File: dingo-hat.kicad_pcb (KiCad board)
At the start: 2 copper layers, 65 x 56 mm, 94 parts, among them J1 LiPo-Power, J10 PJ-038BH, J11 Bypass-Power, J12 Chassis-Out, J13 i2c_display, J14 NEOPIXEL, J15 MPU-9250, J2 Raspberry_Pi_2_3, J201 Bootstrap, J24 3mm_Mount, J25 3mm_Mount, J26 3mm_Mount, J27 3mm_Mount, J3 ULTRA_0, J4 ULTRA_1, J5 LiPo-Balance, J6 0, J7 1, J8 2, J9 3, SW1 GPIO13, U1 MCP3021, U2 PCA9685PW, U201 AP9211, U202 MCP73213T, U203 BQ29209DRBR, U301 AOZ6605PI-1

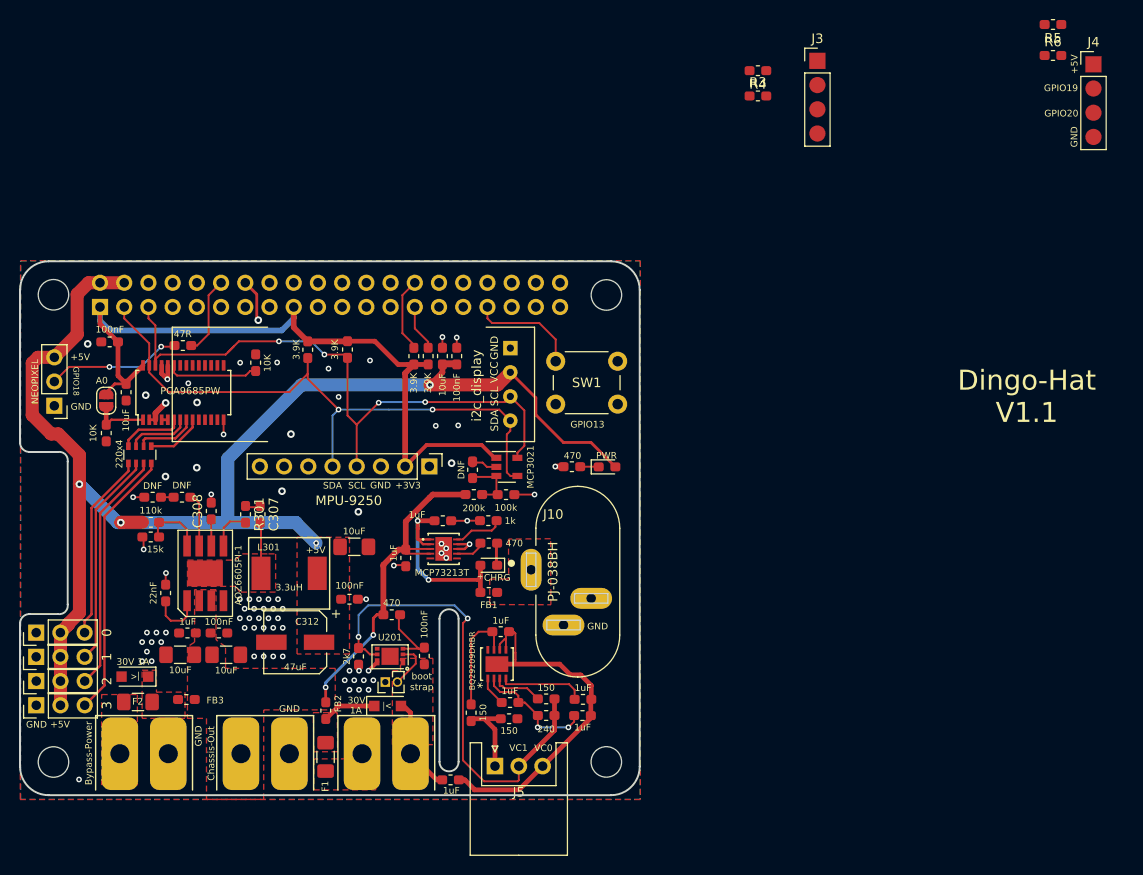
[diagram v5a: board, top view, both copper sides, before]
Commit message: Minor updates to hopefully make soldering easier.
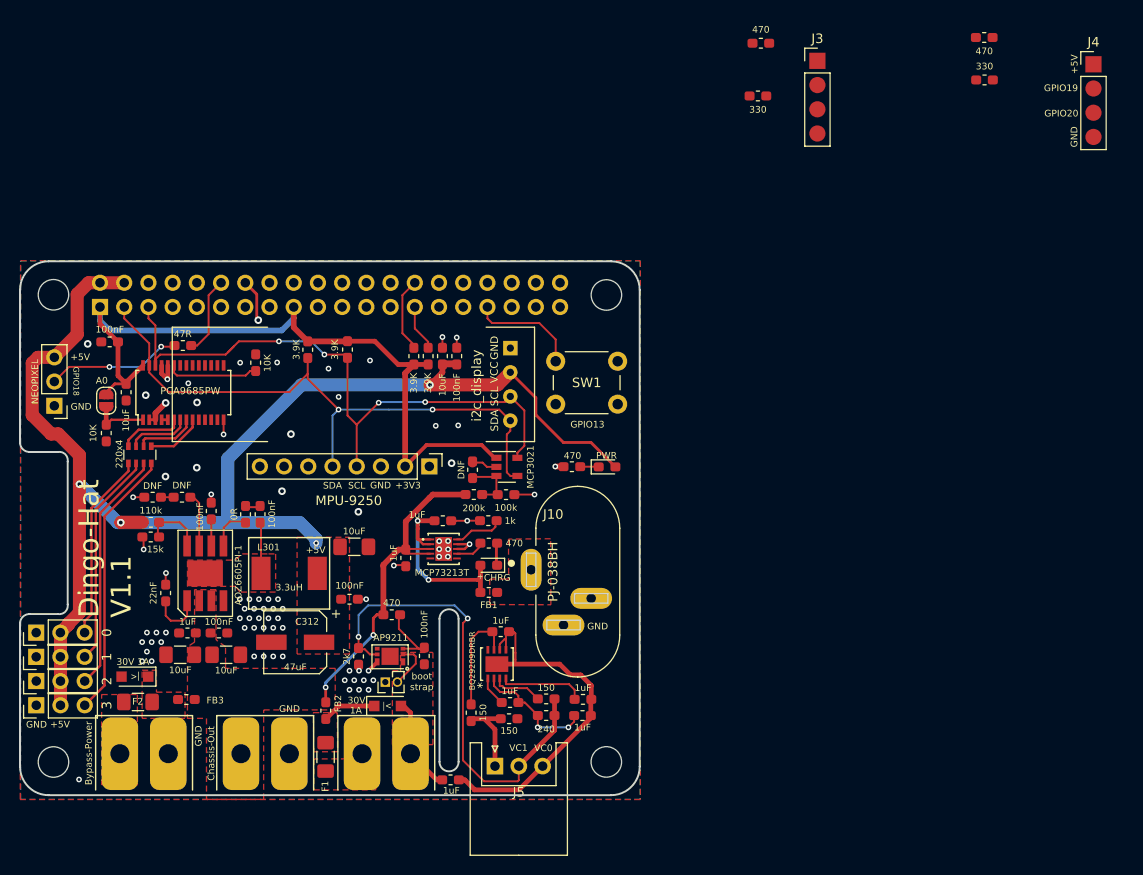
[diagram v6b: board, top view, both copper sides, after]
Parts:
- moved G4 85.2 mm to (186.8, 52.0)
- moved G5 85.2 mm to (186.7, 52.0)
- moved R5 9.24 mm to (201.2, 24.5)
- moved R6 7.45 mm to (201.1, 20.0)
- moved R4 2.90 mm to (177.7, 20.6)
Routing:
- net GND: vias 81 -> 83

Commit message: Tweaks to footprint alignment.
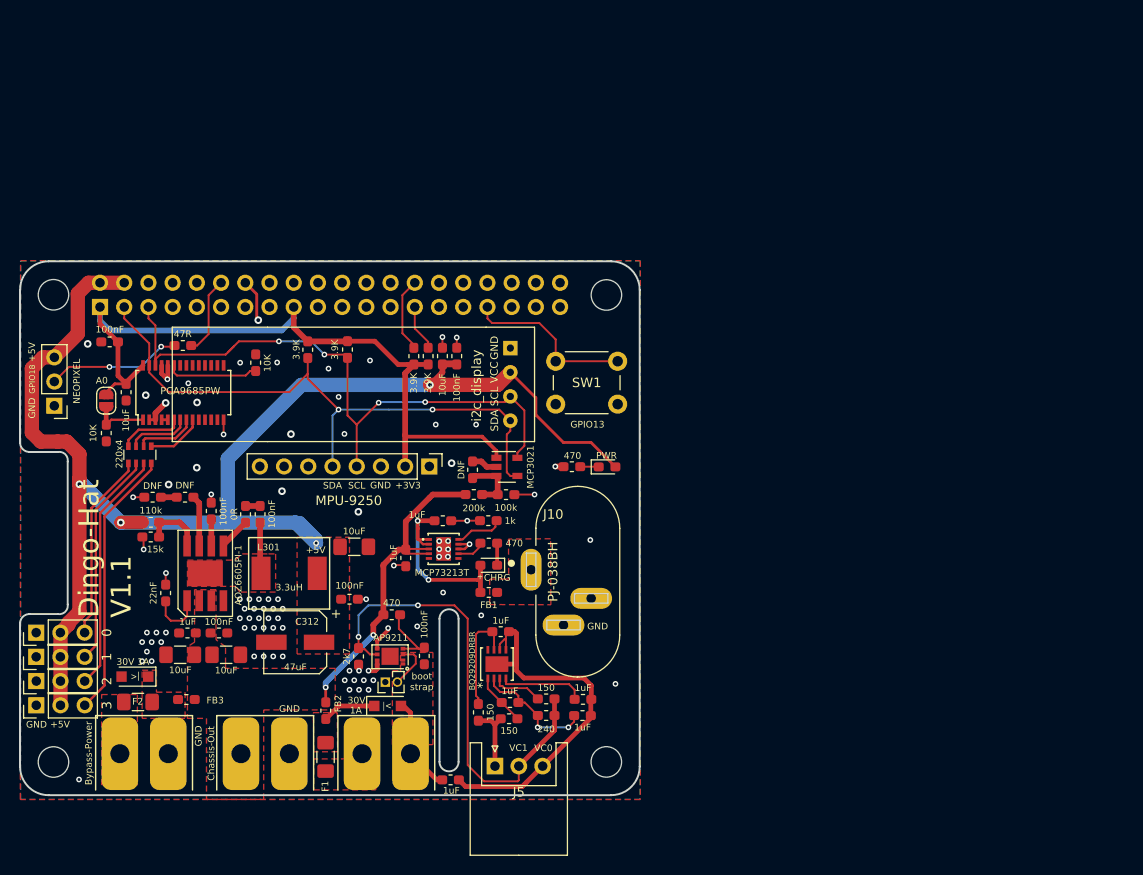
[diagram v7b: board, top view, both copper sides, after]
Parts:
- removed G3: LCA2020Logo.2, libs:logo.LCA.2020.2
- removed J3: ULTRA_0, Connector_PinHeader_2.54mm:PinHeader_1x04_P2.54mm_Vertical
- removed J4: ULTRA_1, Connector_PinHeader_2.54mm:PinHeader_1x04_P2.54mm_Vertical
- removed R3, R5: 330, Resistor_SMD:R_0603_1608Metric_Pad1.05x0.95mm_HandSolder
- removed R4, R6: 470, Resistor_SMD:R_0603_1608Metric_Pad1.05x0.95mm_HandSolder
- moved G1 97.5 mm to (112.0, 72.5)
- moved G5 75.0 mm to (112.0, 58.9)
- moved G2 75.0 mm to (132.4, 56.3)
- moved G4 75.0 mm to (112.1, 58.9)
- moved R208 0.76 mm to (148.1, 90.8)
- moved R302 0.32 mm to (117.3, 68.2)
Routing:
- net +5V: track 146.7 -> 175.7 mm
- net /GPIO13: track 11.6 -> 18.1 mm
- net Net-(C1-Pad1): track 5.61 -> 11.8 mm
- net GND: track 36.0 -> 39.1 mm, vias 83 -> 89
- net /VC2: track 9.97 -> 7.12 mm
- net Net-(C308-Pad1): track 2.92 -> 5.71 mm
- net Net-(C205-Pad1): track 3.13 -> 5.52 mm
- net /VC0: track 41.8 -> 44.0 mm
- net Net-(U201-Pad4): track 0.00 -> 1.53 mm, vias 0 -> 1
- net Net-(R303-Pad2): track 6.63 -> 8.04 mm
- net Net-(R301-Pad2): track 4.50 -> 3.41 mm
- net /BatterySupply: track 36.2 -> 35.6 mm
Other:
- board text removed: "GPIO19"
- board text removed: "GPIO20"

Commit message: New V.1.2 gerbers
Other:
- board text added: "Dingo-Hat V1.2"
- board text removed: "Dingo-Hat V1.1"
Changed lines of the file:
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@@
       (padsonsilk true)
       (subtractmaskfromsilk false)
-      (outputformat 4)
+      (outputformat 1)
       (mirror false)
       (drillshape 0)
       (scaleselection 1)
-      (outputdirectory "pdf/"))
+      (outputdirectory "Gerbers/"))
   )
   (net 0 "")
@@
     (effects (font (size 0.7 0.7) (thickness 0.175)))
   )
-  (gr_text "Dingo-Hat\nV1.1" (at 108.94 80.894 90) (layer F.SilkS)
+  (gr_text "Dingo-Hat\nV1.2" (at 108.94 80.894 90) (layer F.SilkS)
     (effects (font (size 2.1 2.1) (thickness 0.525)) (justify left))
   )
